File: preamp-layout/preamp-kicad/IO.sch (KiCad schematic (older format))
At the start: 14 parts, among them J36 Conn_Coaxial_x2, J37 Conn_Coaxial_x2, J38 Conn_Coaxial_x2, J39 Conn_Coaxial_x2, J40 Conn_Coaxial_x2, J41 Conn_01x03_Female, J42 Conn_01x03_Female, J43 Conn_01x03_Female, J44 Conn_01x03_Female, J45 Conn_01x03_Female, J46 Conn_01x03_Male, J47 Conn_01x03_Male, J48 Conn_Coaxial_x2, J49 Conn_Coaxial_x2

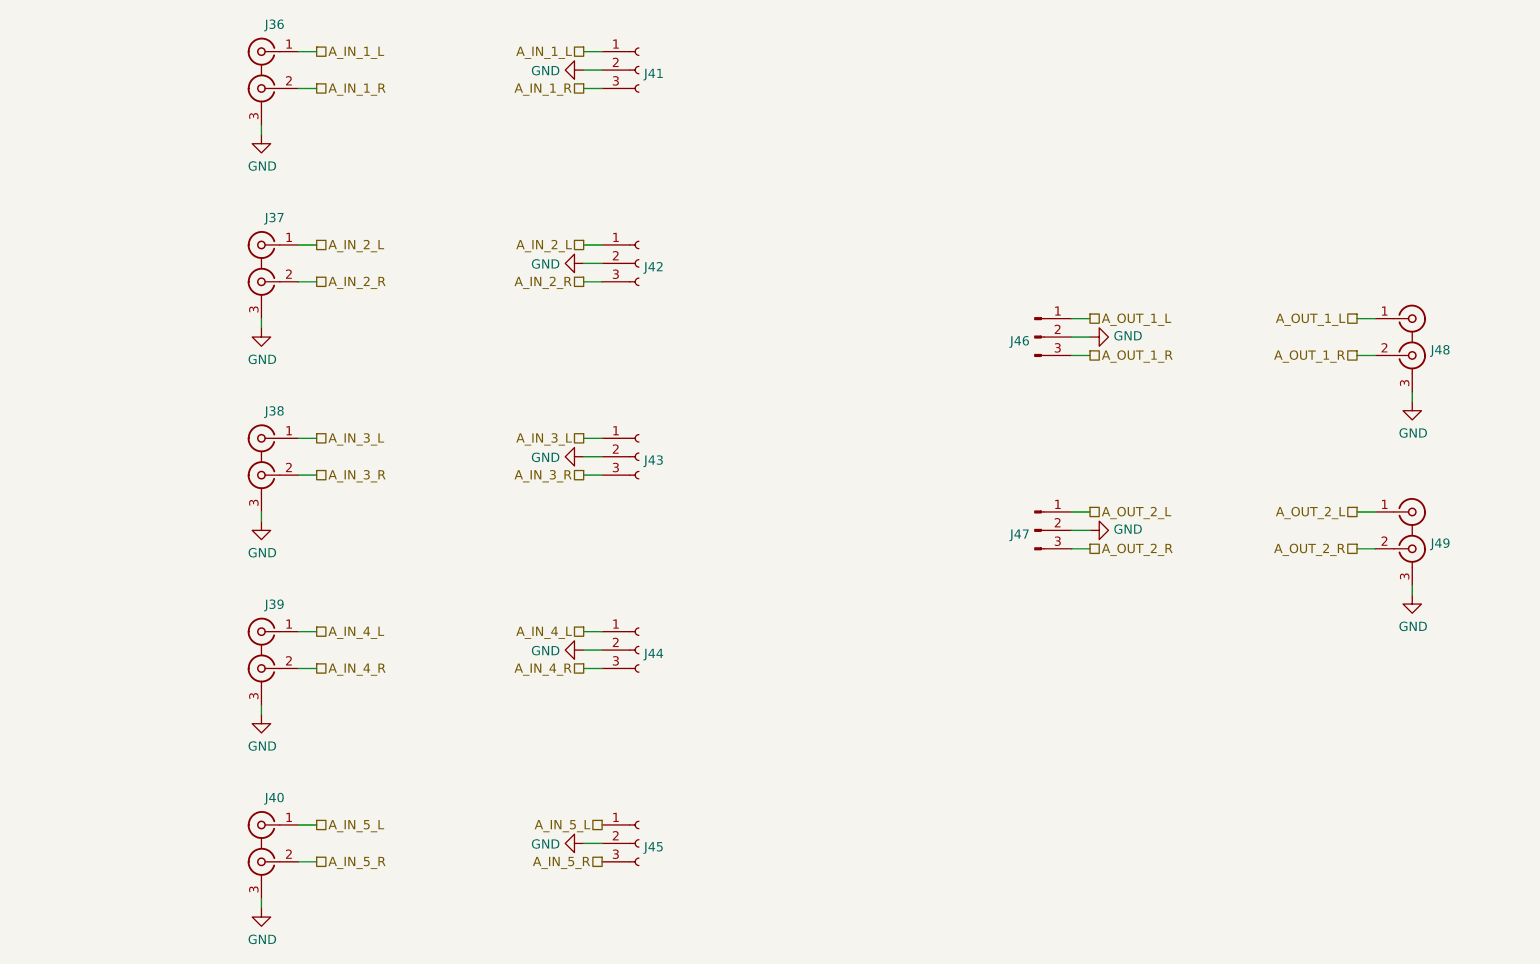
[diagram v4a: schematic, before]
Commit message: RefDes Update
Re-ran refdes assignment, updated BOM accordingly.
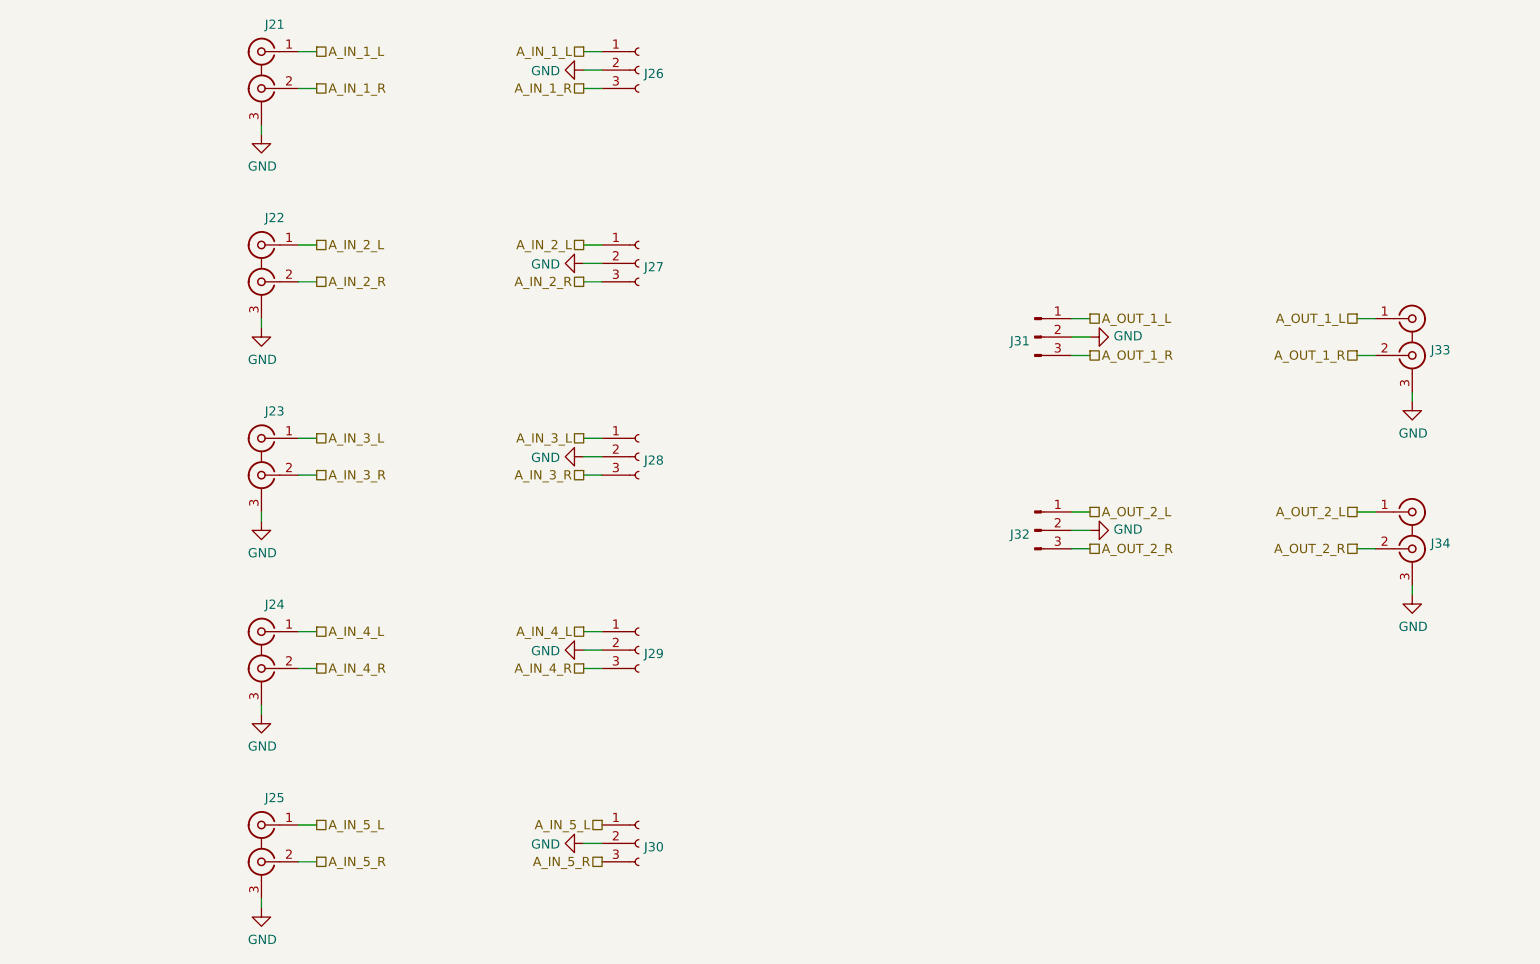
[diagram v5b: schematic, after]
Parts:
- renumbered J36 to J21, J37 to J22, J38 to J23, J39 to J24, J40 to J25, J41 to J26, J42 to J27, J43 to J28, J44 to J29, J45 to J30, J46 to J31, J47 to J32, J48 to J33, J49 to J34
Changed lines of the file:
@@
 P 2800 2850
 AR Path="/5E2D8DA2/5E60DD2B" Ref="J?"  Part="1"
-AR Path="/5E607732/5E60DD2B" Ref="J37"  Part="1"
-F 0 "J37" H 2728 3097 50  0000 C CNN
+AR Path="/5E607732/5E60DD2B" Ref="J22"  Part="1"
+F 0 "J22" H 2728 3097 50  0000 C CNN
 F 1 "Conn_Coaxial_x2" H 2728 3097 50  0001 C CNN
 F 2 "" H 2800 2750 50  0001 C CNN
@@
 $EndComp
 $Comp
-L Connector:Conn_01x03_Female J42
+L Connector:Conn_01x03_Female J27
 U 1 1 5E60DD36
 P 4850 2850
-F 0 "J42" H 4878 2830 50  0000 L CNN
+F 0 "J27" H 4878 2830 50  0000 L CNN
 F 1 "Conn_01x03_Female" H 4878 2785 50  0001 L CNN
 F 2 "Connector_PinHeader_2.54mm:PinHeader_1x03_P2.54mm_Vertical" H 4850 2850 50  0001 C CNN
@@
 P 2800 1800
 AR Path="/5E2D8DA2/6431D3FD" Ref="J?"  Part="1"
-AR Path="/5E607732/6431D3FD" Ref="J36"  Part="1"
-F 0 "J36" H 2728 2047 50  0000 C CNN
+AR Path="/5E607732/6431D3FD" Ref="J21"  Part="1"
+F 0 "J21" H 2728 2047 50  0000 C CNN
 F 1 "Conn_Coaxial_x2" H 2728 2047 50  0001 C CNN
 F 2 "" H 2800 1700 50  0001 C CNN
@@
 $EndComp
 $Comp
-L Connector:Conn_01x03_Female J41
+L Connector:Conn_01x03_Female J26
 U 1 1 6431D407
 P 4850 1800
-F 0 "J41" H 4878 1780 50  0000 L CNN
+F 0 "J26" H 4878 1780 50  0000 L CNN
 F 1 "Conn_01x03_Female" H 4878 1735 50  0001 L CNN
 F 2 "Connector_PinHeader_2.54mm:PinHeader_1x03_P2.54mm_Vertical" H 4850 1800 50  0001 C CNN
@@
 P 2800 4950
 AR Path="/5E2D8DA2/6433171F" Ref="J?"  Part="1"
-AR Path="/5E607732/6433171F" Ref="J39"  Part="1"
-F 0 "J39" H 2728 5197 50  0000 C CNN
+AR Path="/5E607732/6433171F" Ref="J24"  Part="1"
+F 0 "J24" H 2728 5197 50  0000 C CNN
 F 1 "Conn_Coaxial_x2" H 2728 5197 50  0001 C CNN
 F 2 "" H 2800 4850 50  0001 C CNN
@@
 $EndComp
 $Comp
-L Connector:Conn_01x03_Female J44
+L Connector:Conn_01x03_Female J29
 U 1 1 64331729
 P 4850 4950
-F 0 "J44" H 4878 4930 50  0000 L CNN
+F 0 "J29" H 4878 4930 50  0000 L CNN
 F 1 "Conn_01x03_Female" H 4878 4885 50  0001 L CNN
 F 2 "Connector_PinHeader_2.54mm:PinHeader_1x03_P2.54mm_Vertical" H 4850 4950 50  0001 C CNN
@@
 P 2800 3900
 AR Path="/5E2D8DA2/64331754" Ref="J?"  Part="1"
-AR Path="/5E607732/64331754" Ref="J38"  Part="1"
-F 0 "J38" H 2728 4147 50  0000 C CNN
+AR Path="/5E607732/64331754" Ref="J23"  Part="1"
+F 0 "J23" H 2728 4147 50  0000 C CNN
 F 1 "Conn_Coaxial_x2" H 2728 4147 50  0001 C CNN
 F 2 "" H 2800 3800 50  0001 C CNN
@@
 $EndComp
 $Comp
-L Connector:Conn_01x03_Female J43
+L Connector:Conn_01x03_Female J28
 U 1 1 6433175E
 P 4850 3900
-F 0 "J43" H 4878 3880 50  0000 L CNN
+F 0 "J28" H 4878 3880 50  0000 L CNN
 F 1 "Conn_01x03_Female" H 4878 3835 50  0001 L CNN
 F 2 "Connector_PinHeader_2.54mm:PinHeader_1x03_P2.54mm_Vertical" H 4850 3900 50  0001 C CNN
@@
 P 2800 6000
 AR Path="/5E2D8DA2/6433C001" Ref="J?"  Part="1"
-AR Path="/5E607732/6433C001" Ref="J40"  Part="1"
-F 0 "J40" H 2728 6247 50  0000 C CNN
+AR Path="/5E607732/6433C001" Ref="J25"  Part="1"
+F 0 "J25" H 2728 6247 50  0000 C CNN
 F 1 "Conn_Coaxial_x2" H 2728 6247 50  0001 C CNN
 F 2 "" H 2800 5900 50  0001 C CNN
@@
 $EndComp
 $Comp
-L Connector:Conn_01x03_Female J45
+L Connector:Conn_01x03_Female J30
 U 1 1 6433C00B
 P 4850 6000
-F 0 "J45" H 4878 5980 50  0000 L CNN
+F 0 "J30" H 4878 5980 50  0000 L CNN
 F 1 "Conn_01x03_Female" H 4878 5935 50  0001 L CNN
 F 2 "Connector_PinHeader_2.54mm:PinHeader_1x03_P2.54mm_Vertical" H 4850 6000 50  0001 C CNN
@@
 P 9050 4300
 AR Path="/5E2D8DA2/64358093" Ref="J?"  Part="1"
-AR Path="/5E607732/64358093" Ref="J49"  Part="1"
-F 0 "J49" H 9150 4229 50  0000 L CNN
+AR Path="/5E607732/64358093" Ref="J34"  Part="1"
+F 0 "J34" H 9150 4229 50  0000 L CNN
 F 1 "Conn_Coaxial_x2" H 8978 4547 50  0001 C CNN
 F 2 "" H 9050 4200 50  0001 C CNN
@@
 P 9050 3250
 AR Path="/5E2D8DA2/64354C54" Ref="J?"  Part="1"
-AR Path="/5E607732/64354C54" Ref="J48"  Part="1"
-F 0 "J48" H 9150 3179 50  0000 L CNN
+AR Path="/5E607732/64354C54" Ref="J33"  Part="1"
+F 0 "J33" H 9150 3179 50  0000 L CNN
 F 1 "Conn_Coaxial_x2" H 8978 3497 50  0001 C CNN
 F 2 "" H 9050 3150 50  0001 C CNN
@@
 $EndComp
 $Comp
-L Connector:Conn_01x03_Male J46
+L Connector:Conn_01x03_Male J31
 U 1 1 6436D21D
 P 7000 3250
-F 0 "J46" H 6973 3228 50  0000 R CNN
+F 0 "J31" H 6973 3228 50  0000 R CNN
 F 1 "Conn_01x03_Male" H 6972 3183 50  0001 R CNN
 F 2 "Connector_PinHeader_2.54mm:PinHeader_1x03_P2.54mm_Vertical" H 7000 3250 50  0001 C CNN
@@
 $EndComp
 $Comp
-L Connector:Conn_01x03_Male J47
+L Connector:Conn_01x03_Male J32
 U 1 1 6437A2AD
 P 7000 4300
-F 0 "J47" H 6973 4278 50  0000 R CNN
+F 0 "J32" H 6973 4278 50  0000 R CNN
 F 1 "Conn_01x03_Male" H 6972 4233 50  0001 R CNN
 F 2 "Connector_PinHeader_2.54mm:PinHeader_1x03_P2.54mm_Vertical" H 7000 4300 50  0001 C CNN
@@
 P 4550 1800
 AR Path="/5E26F6FE/64B8A4E5" Ref="#PWR?"  Part="1"
-AR Path="/5E607732/64B8A4E5" Ref="#PWR040"  Part="1"
-F 0 "#PWR040" H 4550 1550 50  0001 C CNN
+AR Path="/5E607732/64B8A4E5" Ref="#PWR032"  Part="1"
+F 0 "#PWR032" H 4550 1550 50  0001 C CNN
 F 1 "GND" V 4555 1672 50  0000 R CNN
 F 2 "" H 4550 1800 50  0001 C CNN
@@
 P 4550 2850
 AR Path="/5E26F6FE/64B99929" Ref="#PWR?"  Part="1"
-AR Path="/5E607732/64B99929" Ref="#PWR041"  Part="1"
-F 0 "#PWR041" H 4550 2600 50  0001 C CNN
+AR Path="/5E607732/64B99929" Ref="#PWR033"  Part="1"
+F 0 "#PWR033" H 4550 2600 50  0001 C CNN
 F 1 "GND" V 4555 2722 50  0000 R CNN
 F 2 "" H 4550 2850 50  0001 C CNN
@@
 P 4550 3900
 AR Path="/5E26F6FE/64B9AE8F" Ref="#PWR?"  Part="1"
-AR Path="/5E607732/64B9AE8F" Ref="#PWR042"  Part="1"
-F 0 "#PWR042" H 4550 3650 50  0001 C CNN
+AR Path="/5E607732/64B9AE8F" Ref="#PWR034"  Part="1"
+F 0 "#PWR034" H 4550 3650 50  0001 C CNN
 F 1 "GND" V 4555 3772 50  0000 R CNN
 F 2 "" H 4550 3900 50  0001 C CNN
@@
 P 4550 6000
 AR Path="/5E26F6FE/64B9C67B" Ref="#PWR?"  Part="1"
-AR Path="/5E607732/64B9C67B" Ref="#PWR044"  Part="1"
-F 0 "#PWR044" H 4550 5750 50  0001 C CNN
+AR Path="/5E607732/64B9C67B" Ref="#PWR036"  Part="1"
+F 0 "#PWR036" H 4550 5750 50  0001 C CNN
 F 1 "GND" V 4555 5872 50  0000 R CNN
 F 2 "" H 4550 6000 50  0001 C CNN
@@
 P 4550 4950
 AR Path="/5E26F6FE/64B9F2DA" Ref="#PWR?"  Part="1"
-AR Path="/5E607732/64B9F2DA" Ref="#PWR043"  Part="1"
-F 0 "#PWR043" H 4550 4700 50  0001 C CNN
+AR Path="/5E607732/64B9F2DA" Ref="#PWR035"  Part="1"
+F 0 "#PWR035" H 4550 4700 50  0001 C CNN
 F 1 "GND" V 4555 4822 50  0000 R CNN
 F 2 "" H 4550 4950 50  0001 C CNN
@@
 P 7300 3250
 AR Path="/5E26F6FE/64BA0A7B" Ref="#PWR?"  Part="1"
-AR Path="/5E607732/64BA0A7B" Ref="#PWR045"  Part="1"
-F 0 "#PWR045" H 7300 3000 50  0001 C CNN
+AR Path="/5E607732/64BA0A7B" Ref="#PWR037"  Part="1"
+F 0 "#PWR037" H 7300 3000 50  0001 C CNN
 F 1 "GND" V 7305 3122 50  0000 R CNN
 F 2 "" H 7300 3250 50  0001 C CNN
@@
 P 7300 4300
 AR Path="/5E26F6FE/64BA2069" Ref="#PWR?"  Part="1"
-AR Path="/5E607732/64BA2069" Ref="#PWR046"  Part="1"
-F 0 "#PWR046" H 7300 4050 50  0001 C CNN
+AR Path="/5E607732/64BA2069" Ref="#PWR038"  Part="1"
+F 0 "#PWR038" H 7300 4050 50  0001 C CNN
 F 1 "GND" V 7305 4172 50  0000 R CNN
 F 2 "" H 7300 4300 50  0001 C CNN
@@
 P 2800 2150
 AR Path="/5E26F6FE/64BB2C61" Ref="#PWR?"  Part="1"
-AR Path="/5E607732/64BB2C61" Ref="#PWR035"  Part="1"
-F 0 "#PWR035" H 2800 1900 50  0001 C CNN
+AR Path="/5E607732/64BB2C61" Ref="#PWR027"  Part="1"
+F 0 "#PWR027" H 2800 1900 50  0001 C CNN
 F 1 "GND" H 2805 1977 50  0000 C CNN
 F 2 "" H 2800 2150 50  0001 C CNN
@@
 P 9050 4650
 AR Path="/5E26F6FE/5E790D2A" Ref="#PWR?"  Part="1"
-AR Path="/5E607732/5E790D2A" Ref="#PWR0110"  Part="1"
-F 0 "#PWR0110" H 9050 4400 50  0001 C CNN
+AR Path="/5E607732/5E790D2A" Ref="#PWR040"  Part="1"
+F 0 "#PWR040" H 9050 4400 50  0001 C CNN
 F 1 "GND" H 9055 4477 50  0000 C CNN
 F 2 "" H 9050 4650 50  0001 C CNN
@@
 P 2800 3200
 AR Path="/5E26F6FE/5E792160" Ref="#PWR?"  Part="1"
-AR Path="/5E607732/5E792160" Ref="#PWR047"  Part="1"
-F 0 "#PWR047" H 2800 2950 50  0001 C CNN
+AR Path="/5E607732/5E792160" Ref="#PWR028"  Part="1"
+F 0 "#PWR028" H 2800 2950 50  0001 C CNN
 F 1 "GND" H 2805 3027 50  0000 C CNN
 F 2 "" H 2800 3200 50  0001 C CNN
@@
 P 2800 4250
 AR Path="/5E26F6FE/5E792F4E" Ref="#PWR?"  Part="1"
-AR Path="/5E607732/5E792F4E" Ref="#PWR048"  Part="1"
-F 0 "#PWR048" H 2800 4000 50  0001 C CNN
+AR Path="/5E607732/5E792F4E" Ref="#PWR029"  Part="1"
+F 0 "#PWR029" H 2800 4000 50  0001 C CNN
 F 1 "GND" H 2805 4077 50  0000 C CNN
 F 2 "" H 2800 4250 50  0001 C CNN
@@
 P 2800 5300
 AR Path="/5E26F6FE/5E7942CF" Ref="#PWR?"  Part="1"
-AR Path="/5E607732/5E7942CF" Ref="#PWR098"  Part="1"
-F 0 "#PWR098" H 2800 5050 50  0001 C CNN
+AR Path="/5E607732/5E7942CF" Ref="#PWR030"  Part="1"
+F 0 "#PWR030" H 2800 5050 50  0001 C CNN
 F 1 "GND" H 2805 5127 50  0000 C CNN
 F 2 "" H 2800 5300 50  0001 C CNN
@@
 P 2800 6350
 AR Path="/5E26F6FE/5E795042" Ref="#PWR?"  Part="1"
-AR Path="/5E607732/5E795042" Ref="#PWR0100"  Part="1"
-F 0 "#PWR0100" H 2800 6100 50  0001 C CNN
+AR Path="/5E607732/5E795042" Ref="#PWR031"  Part="1"
+F 0 "#PWR031" H 2800 6100 50  0001 C CNN
 F 1 "GND" H 2805 6177 50  0000 C CNN
 F 2 "" H 2800 6350 50  0001 C CNN
@@
 P 9050 3600
 AR Path="/5E26F6FE/5E7983F2" Ref="#PWR?"  Part="1"
-AR Path="/5E607732/5E7983F2" Ref="#PWR0109"  Part="1"
-F 0 "#PWR0109" H 9050 3350 50  0001 C CNN
+AR Path="/5E607732/5E7983F2" Ref="#PWR039"  Part="1"
+F 0 "#PWR039" H 9050 3350 50  0001 C CNN
 F 1 "GND" H 9055 3427 50  0000 C CNN
 F 2 "" H 9050 3600 50  0001 C CNN

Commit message: Periodic backup
Extensive changes as a result of PCB layout phase.
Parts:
- removed J26, J27, J28, J29, J30: Conn_01x03_Female, Connector_PinHeader_2.54mm:PinHeader_1x03_P2.54mm_Vertical, symbol Connector:Conn_01x03_Female
- removed J31, J32: Conn_01x03_Male, Connector_PinHeader_2.54mm:PinHeader_1x03_P2.54mm_Vertical, symbol Connector:Conn_01x03_Male
- added J28: Conn_01x18_Female, Connector_PinSocket_2.54mm:PinSocket_1x18_P2.54mm_Vertical, symbol Connector:Conn_01x18_Female
- added J29: Conn_01x08_Female, Connector_PinSocket_2.54mm:PinSocket_1x08_P2.54mm_Vertical, symbol Connector:Conn_01x08_Female
- added J45, J46, J85, J90: Conn_Coaxial_x2, symbol Connector:Conn_Coaxial_x2
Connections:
- net A_IN_1_L: now also J28.2 (Pin_2)
- net A_IN_1_R: now also J28.3 (Pin_3)
- net A_IN_2_L: now also J28.4 (Pin_4)
- net A_IN_2_R: now also J28.5 (Pin_5)
- net A_IN_3_L: now also J28.6 (Pin_6)
- net A_IN_3_R: now also J28.7 (Pin_7)
- net A_IN_4_L: now also J28.8 (Pin_8)
- net A_IN_4_R: now also J28.9 (Pin_9)
- net A_IN_5_L: now also J28.10 (Pin_10)
- net A_IN_5_R: now also J28.11 (Pin_11)
- net A_OUT_1_L: now also J29.2 (Pin_2)
- net A_OUT_1_R: now also J29.3 (Pin_3)
- net A_OUT_2_L: now also J29.4 (Pin_4)
- net A_OUT_2_R: now also J29.5 (Pin_5)
- net GND: now also J28.1 (Pin_1), J28.18 (Pin_18), J29.1 (Pin_1), J29.8 (Pin_8), J45.3 (EXT), J46.3 (EXT), J85.3 (EXT), J90.3 (EXT)
- new net A_IN_6_L: J28.12 (Pin_12), J45.1 (IN1)
- new net A_IN_6_R: J28.13 (Pin_13), J45.2 (IN2)
- new net A_IN_7_L: J28.14 (Pin_14), J46.1 (IN1)
- new net A_IN_7_R: J28.15 (Pin_15), J46.2 (IN2)
- new net A_IN_8_L: J28.16 (Pin_16), J85.1 (IN1)
- new net A_IN_8_R: J28.17 (Pin_17), J85.2 (IN2)
- new net A_OUT_3_L: J29.6 (Pin_6), J90.1 (IN1)
- new net A_OUT_3_R: J29.7 (Pin_7), J90.2 (IN2)
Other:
- moved on the sheet: J21, J22, J23, J24, J25, J33, J34

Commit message: PCB layout
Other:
- moved on the sheet: J28
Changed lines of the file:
@@
 	1    0    0    -1
 $EndComp
-Text HLabel 4900 3650 0    50   UnSpc ~ 0
-A_IN_5_R
-Text HLabel 4900 3550 0    50   UnSpc ~ 0
-A_IN_5_L
 Wire Wire Line
 	3100 2000 3200 2000
@@
 Wire Wire Line
 	2900 5350 2900 5400
-Text HLabel 4900 4250 0    50   UnSpc ~ 0
-A_IN_8_R
-Text HLabel 4900 4150 0    50   UnSpc ~ 0
-A_IN_8_L
-Wire Wire Line
-	4900 4250 5000 4250
-Wire Wire Line
-	4900 4150 5000 4150
-Text HLabel 4900 4050 0    50   UnSpc ~ 0
-A_IN_7_R
-Text HLabel 4900 3950 0    50   UnSpc ~ 0
-A_IN_7_L
-Wire Wire Line
-	4900 4050 5000 4050
-Wire Wire Line
-	4900 3950 5000 3950
-Wire Wire Line
-	4900 3850 5000 3850
-Wire Wire Line
-	4900 3750 5000 3750
-Text HLabel 4900 3850 0    50   UnSpc ~ 0
-A_IN_6_R
-Text HLabel 4900 3750 0    50   UnSpc ~ 0
-A_IN_6_L
 Text HLabel 3200 5150 2    50   UnSpc ~ 0
 A_IN_8_R
-Wire Wire Line
-	4900 3650 5000 3650
-Wire Wire Line
-	4900 3550 5000 3550
-Wire Wire Line
-	4900 3350 5000 3350
-Wire Wire Line
-	4900 3450 5000 3450
-Text HLabel 4900 3350 0    50   UnSpc ~ 0
-A_IN_4_L
-Text HLabel 4900 3450 0    50   UnSpc ~ 0
-A_IN_4_R
 Wire Wire Line
 	1750 5150 1850 5150
@@
 A_IN_4_L
 Wire Wire Line
-	4900 3150 5000 3150
-Wire Wire Line
-	4900 3250 5000 3250
-Text HLabel 4900 3150 0    50   UnSpc ~ 0
-A_IN_3_L
-Text HLabel 4900 3250 0    50   UnSpc ~ 0
-A_IN_3_R
-Wire Wire Line
 	1750 4100 1850 4100
 Wire Wire Line
@@
 A_IN_3_L
 Wire Wire Line
-	4900 2950 5000 2950
-Wire Wire Line
-	4900 3050 5000 3050
-Wire Wire Line
 	1750 3050 1850 3050
 Wire Wire Line
 	1750 2850 1850 2850
-Text HLabel 4900 2950 0    50   UnSpc ~ 0
-A_IN_2_L
-Text HLabel 4900 3050 0    50   UnSpc ~ 0
-A_IN_2_R
 Text HLabel 1850 3050 2    50   UnSpc ~ 0
 A_IN_2_R
@@
 Wire Wire Line
 	1750 2000 1850 2000
-Wire Wire Line
-	4900 2850 5000 2850
-Wire Wire Line
-	4900 2750 5000 2750
-Text HLabel 4900 2750 0    50   UnSpc ~ 0
-A_IN_1_L
-Text HLabel 4900 2850 0    50   UnSpc ~ 0
-A_IN_1_R
 Text HLabel 1850 2000 2    50   UnSpc ~ 0
 A_IN_1_R
@@
 L Connector:Conn_01x18_Female J28
 U 1 1 5EF67BC3
-P 5200 3450
-F 0 "J28" H 5228 3380 50  0000 L CNN
-F 1 "Conn_01x18_Female" H 5228 3335 50  0001 L CNN
-F 2 "Connector_PinSocket_2.54mm:PinSocket_1x18_P2.54mm_Vertical" H 5200 3450 50  0001 C CNN
-F 3 "~" H 5200 3450 50  0001 C CNN
-	1    5200 3450
-	1    0    0    -1
-$EndComp
-Wire Wire Line
-	5000 2650 4900 2650
+P 6000 3550
+F 0 "J28" H 6028 3480 50  0000 L CNN
+F 1 "Conn_01x18_Female" H 6028 3435 50  0001 L CNN
+F 2 "Connector_PinSocket_2.54mm:PinSocket_1x18_P2.54mm_Vertical" H 6000 3550 50  0001 C CNN
+F 3 "~" H 6000 3550 50  0001 C CNN
+	1    6000 3550
+	1    0    0    -1
+$EndComp
+Wire Wire Line
+	5800 2750 5700 2750
 $Comp
 L power:GND #PWR?
 U 1 1 5EF7F944
-P 4900 2650
+P 5700 2750
 AR Path="/5E26F6FE/5EF7F944" Ref="#PWR?"  Part="1"
 AR Path="/5E607732/5EF7F944" Ref="#PWR036"  Part="1"
-F 0 "#PWR036" H 4900 2400 50  0001 C CNN
-F 1 "GND" V 4905 2522 50  0000 R CNN
-F 2 "" H 4900 2650 50  0001 C CNN
-F 3 "" H 4900 2650 50  0001 C CNN
-	1    4900 2650
+F 0 "#PWR036" H 5700 2500 50  0001 C CNN
+F 1 "GND" V 5705 2622 50  0000 R CNN
+F 2 "" H 5700 2750 50  0001 C CNN
+F 3 "" H 5700 2750 50  0001 C CNN
+	1    5700 2750
 	0    1    1    0
 $EndComp
 Wire Wire Line
-	5000 4350 4900 4350
+	5800 4450 5700 4450
 $Comp
 L power:GND #PWR?
 U 1 1 5EF814C3
-P 4900 4350
+P 5700 4450
 AR Path="/5E26F6FE/5EF814C3" Ref="#PWR?"  Part="1"
 AR Path="/5E607732/5EF814C3" Ref="#PWR037"  Part="1"
-F 0 "#PWR037" H 4900 4100 50  0001 C CNN
-F 1 "GND" V 4905 4222 50  0000 R CNN
-F 2 "" H 4900 4350 50  0001 C CNN
-F 3 "" H 4900 4350 50  0001 C CNN
-	1    4900 4350
+F 0 "#PWR037" H 5700 4200 50  0001 C CNN
+F 1 "GND" V 5705 4322 50  0000 R CNN
+F 2 "" H 5700 4450 50  0001 C CNN
+F 3 "" H 5700 4450 50  0001 C CNN
+	1    5700 4450
 	0    1    1    0
 $EndComp
@@
 	0    -1   -1   0
 $EndComp
+Wire Wire Line
+	5700 2850 5800 2850
+Wire Wire Line
+	5700 2950 5800 2950
+Wire Wire Line
+	5700 3050 5800 3050
+Wire Wire Line
+	5700 3150 5800 3150
+Wire Wire Line
+	5700 3250 5800 3250
+Wire Wire Line
+	5700 3350 5800 3350
+Wire Wire Line
+	5700 3450 5800 3450
+Wire Wire Line
+	5700 3550 5800 3550
+Wire Wire Line
+	5700 4350 5800 4350
+Wire Wire Line
+	5700 4250 5800 4250
+Wire Wire Line
+	5700 4150 5800 4150
+Wire Wire Line
+	5700 4050 5800 4050
+Wire Wire Line
+	5700 3950 5800 3950
+Wire Wire Line
+	5700 3850 5800 3850
+Wire Wire Line
+	5700 3750 5800 3750
+Wire Wire Line
+	5700 3650 5800 3650
+Text HLabel 5300 3650 0    50   UnSpc ~ 0
+A_IN_1_R
+Text HLabel 5300 2850 0    50   UnSpc ~ 0
+A_IN_1_L
+Text HLabel 5300 3750 0    50   UnSpc ~ 0
+A_IN_2_R
+Text HLabel 5300 2950 0    50   UnSpc ~ 0
+A_IN_2_L
+Text HLabel 5300 3850 0    50   UnSpc ~ 0
+A_IN_3_R
+Text HLabel 5300 3050 0    50   UnSpc ~ 0
+A_IN_3_L
+Text HLabel 5300 3950 0    50   UnSpc ~ 0
+A_IN_4_R
+Text HLabel 5300 3150 0    50   UnSpc ~ 0
+A_IN_4_L
+Text HLabel 5300 3450 0    50   UnSpc ~ 0
+A_IN_6_L
+Text HLabel 5300 4250 0    50   UnSpc ~ 0
+A_IN_6_R
+Text HLabel 5300 3350 0    50   UnSpc ~ 0
+A_IN_7_L
+Text HLabel 5300 4150 0    50   UnSpc ~ 0
+A_IN_7_R
+Text HLabel 5300 3250 0    50   UnSpc ~ 0
+A_IN_8_L
+Text HLabel 5300 4050 0    50   UnSpc ~ 0
+A_IN_8_R
+Text HLabel 5300 3550 0    50   UnSpc ~ 0
+A_IN_5_L
+Text HLabel 5300 4350 0    50   UnSpc ~ 0
+A_IN_5_R
 $EndSCHEMATC
